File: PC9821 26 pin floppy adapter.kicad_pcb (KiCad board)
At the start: 2 copper layers, 31 x 59 mm, 7 parts

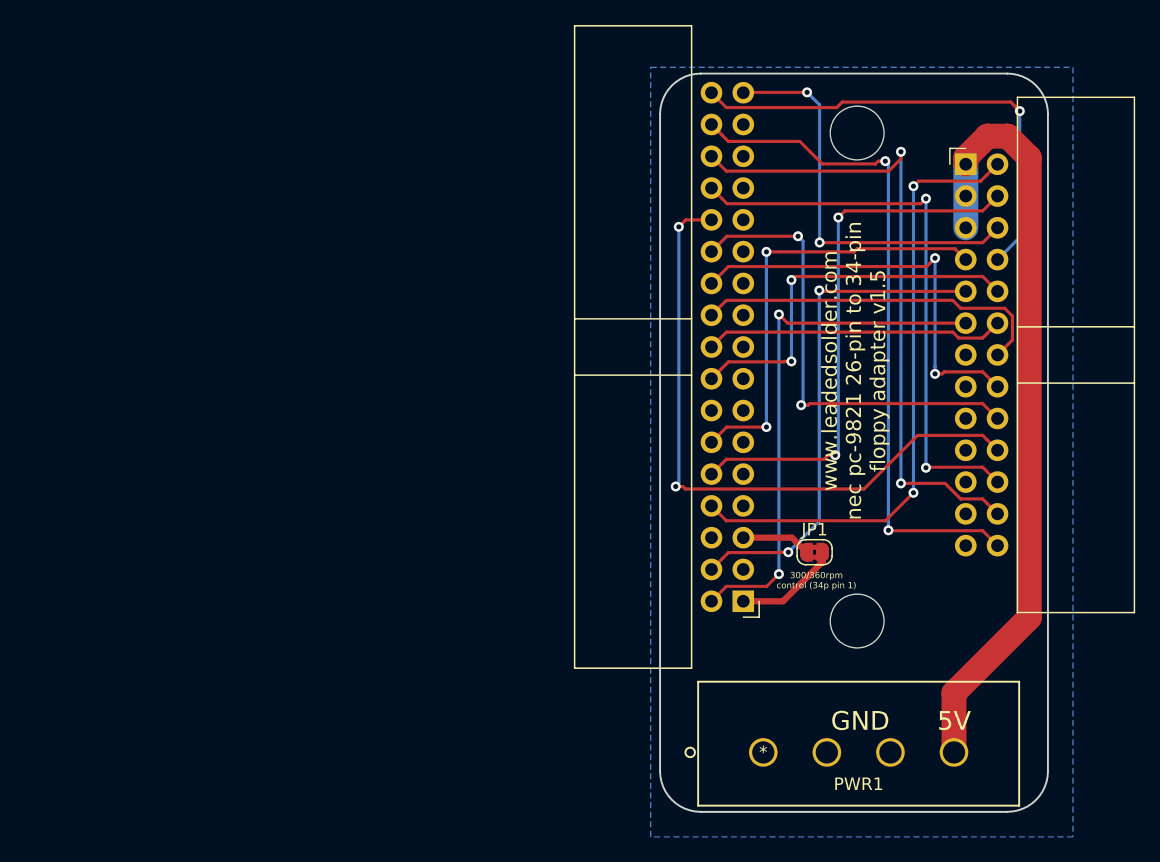
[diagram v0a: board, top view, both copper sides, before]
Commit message: V2.0: Floppy cable variant to support two drives
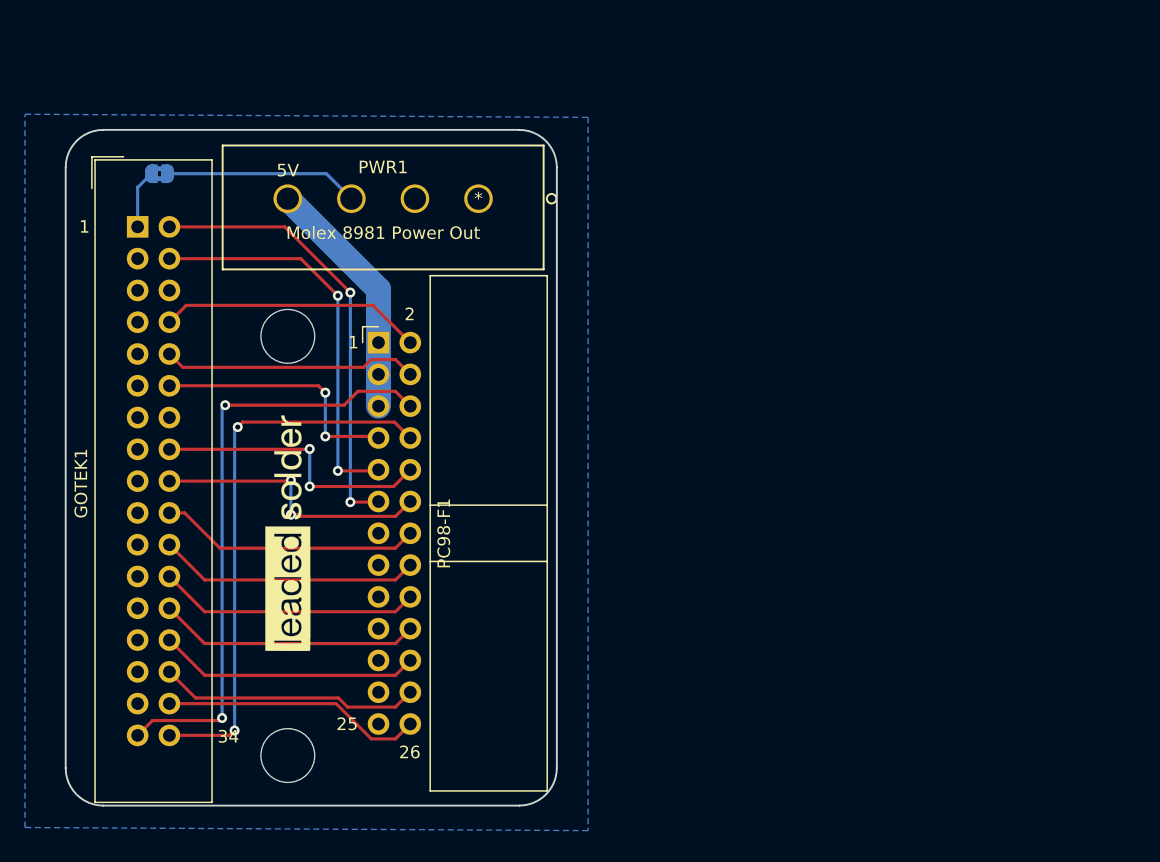
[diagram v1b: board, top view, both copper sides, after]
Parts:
- removed the REF** at (161.5, 84.5)
- removed the REF** at (161.5, 123.5)
- added G***: LOGO, Logos:leaded-solder-logo-800dpi, F.Cu at (116.0, 116.5)
- added REF**: MountingHole_4.3mm_M4_DIN965, MountingHole:MountingHole_4.3mm_M4_DIN965, F.Cu at (116.0, 134.2)
- added REF**: MountingHole_4.3mm_M4_DIN965, MountingHole:MountingHole_4.3mm_M4_DIN965, F.Cu at (116.0, 100.8)
- GOTEK1: value 34-pin female IDC to Gotek -> 34-pin female IDC to standard PC floppy cable; footprint Connector_IDC:IDC-Header_2x17_P2.54mm_Horizontal -> Connector_IDC:IDC-Header_2x17_P2.54mm_Vertical
- JP1: moved to B.Cu
- moved JP1 60.5 mm to (105.8, 87.8), turned to 180 degrees
- moved GOTEK1 56.9 mm to (104.0, 92.0), turned to 0 degrees
- moved PWR1 49.8 mm to (131.2, 89.8), turned to 0 degrees
- moved PC98-F1 49.0 mm to (123.2, 101.2)
- moved G*** 44.3 mm to (115.5, 114.0)
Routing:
- net /+5V_1: track 62.1 -> 19.6 mm
- net /SIDE: track 54.1 -> 20.9 mm, vias 2 -> 0
- net /READ_DATA: track 51.8 -> 20.9 mm, vias 2 -> 0
- net /TRACK_00: track 51.8 -> 20.9 mm, vias 2 -> 0
- net /INDEX_OUT: track 49.5 -> 21.0 mm, vias 2 -> 0
- net /WRITE_PROTECT: track 45.6 -> 20.9 mm, vias 2 -> 0
- net /DRV_SELECT_0: track 43.0 -> 20.4 mm, vias 2 -> 0
- net /WRITE_ENABLE: track 37.4 -> 20.9 mm, vias 2 -> 0
- net /DISK_CHANGE: track 32.6 -> 48.2 mm
- net /DRV_SELECT_1: track 35.3 -> 20.5 mm
- net /WRITE_DATA: track 33.5 -> 20.9 mm, vias 2 -> 0
- net /GND: track 5.53 -> 15.5 mm
- net /HEAD_LOAD: track 40.4 -> 32.0 mm
- net /STEP_PULSE: track 28.7 -> 20.9 mm
- net /MOTOR_ON: track 30.5 -> 22.8 mm
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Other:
- board size 31 x 59 mm -> 39.2 x 54 mm
- board text added: "2"
- board text added: "26"
- board text added: "34"
- board text added: "leadedsolder.com 2018–2022 NEC PC-9821 26-pin to 34-pin floppy adapter v2.0"
- board text removed: "300/360rpm control (34p pin 1)"
- board text removed: "33"
- board text removed: "GND"
- board text removed: "www.leadedsolder.com nec pc-9821 26-pin to 34-pin floppy adapter v1.5"

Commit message: Indicators
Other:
- board text added: "mount this side"
- board text added: "notch this way"
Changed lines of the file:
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@@
   (general
     (thickness 1.6)
-    (drawings 16)
+    (drawings 18)
     (tracks 97)
     (zones 0)
@@
       (xy 3.637322 9.345089) (xy 3.651603 9.3472) (xy 3.724137 9.310413)) (layer B.SilkS) (width 0.01))
   )
+  (gr_text "mount this side" (at 135.5 116.75 90) (layer F.SilkS)
+    (effects (font (size 1 1) (thickness 0.15)))
+  )
+  (gr_text "notch this way" (at 99.5 130.5 90) (layer F.SilkS)
+    (effects (font (size 1 1) (thickness 0.15)))
+  )
   (gr_text "leadedsolder.com 2018–2022\nNEC PC-9821 26-pin to 34-pin\nfloppy adapter v2.0" (at 132 116.5 90) (layer B.SilkS)

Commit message: KiCad 8
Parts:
- JP1: value 300/360 control -> Jumper_2_Bridged
- moved JP1 0.36 mm to (105.4, 87.6)
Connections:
- PWR1 pad 1: Net-(PWR1-Pad1) -> unconnected-(PWR1-Pin_1-Pad1)
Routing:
- net /DRV_SELECT_0: track 20.4 -> 23.3 mm
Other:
- net class Default removed
- board text added: "leadedsolder.com 2018–2024 NEC PC-9821 26-pin to 34-pin floppy adapter v2.0"
- board text removed: "leadedsolder.com 2018–2022 NEC PC-9821 26-pin to 34-pin floppy adapter v2.0"

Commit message: V2 plot settings
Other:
- rule pad_to_mask_clearance: 0.2 -> 0
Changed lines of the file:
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@@
 	)
 	(setup
-		(pad_to_mask_clearance 0.2)
+		(pad_to_mask_clearance 0)
 		(allow_soldermask_bridges_in_footprints no)
 		(pcbplotparams
@@
 			(drillshape 0)
 			(scaleselection 1)
-			(outputdirectory "v2.0")
+			(outputdirectory "pc9821-26p-floppy-v2")
 		)
 	)
